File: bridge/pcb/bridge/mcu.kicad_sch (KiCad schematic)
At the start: 12 parts, among them Q1 PMOS, Q2 PMOS, Q3 PMOS, Q4 PMOS, Q5 PMOS, U1 YAAJ_BluePill

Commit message: Fixed issues, added DAC
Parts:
- added R10: 1k5, Resistor_THT:R_Axial_DIN0309_L9.0mm_D3.2mm_P12.70mm_Horizontal, symbol Device:R
- added U3: AD557JN, bridge:AD557JN, symbol bridge:AD557JN
- Q1, Q2, Q3, Q4, Q5: footprint Package_TO_SOT_THT:TO-3P-3_Horizontal_TabDown -> Package_TO_SOT_THT:TO-220-3_Horizontal_TabDown
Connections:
- net +5V: now also U3.11 (+VCC)
- net GND: now also U3.10 (CS*), U3.12 (GND), U3.13 (GND), U3.9 (CE*)
- net at U1.25 (PA0): now also U3.8 ((MSB)BIT1)
- net at U1.26 (PA1): now also U3.7 (BIT2)
- net at U1.27 (PA2): now also U3.6 (BIT3)
- net at U1.28 (PA3): now also U3.5 (BIT4)
- net at U1.29 (PA4): now also U3.4 (BIT5)
- net at U1.30 (PA5): now also U3.3 (BIT6)
- net at U1.31 (PA6): now also U3.2 (BIT7)
- net at U1.32 (PA7): now also U3.1 ((LSB)BIT8)
- new net: R10.2, U3.14 (VOUTSENSEB), U3.15 (VOUTSENSEA)
- new net ACCEL_AUTO: R10.1, U3.16 (VOUT)
- no-connect marks 30 -> 22

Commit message: Completed schematic
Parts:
- R1, R10, R2, R3, R4, R5: footprint Resistor_THT:R_Axial_DIN0309_L9.0mm_D3.2mm_P12.70mm_Horizontal -> bridge:THT_RESISTOR_WITH_VALUE
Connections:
- net MAN_AUTO_STATE: now reaches U1.11 (PB3)
- no-connect marks 22 -> 21
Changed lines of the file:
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@@
   (no_connect (at 130.81 46.99))
   (no_connect (at 90.17 57.15))
-  (no_connect (at 90.17 64.77))
   (no_connect (at 130.81 74.93))
   (no_connect (at 130.81 44.45))
@@
     )
   )
+  (global_label "MAN_AUTO_STATE" (shape input) (at 90.17 64.77 180) (fields_autoplaced)
+    (effects (font (size 1.27 1.27) bold) (justify right))
+    (property "Intersheetrefs" "${INTERSHEET_REFS}" (at 70.8036 64.77 0)
+      (effects (font (size 1.27 1.27)) (justify right) hide)
+    )
+  )
   (global_label "MCU_START" (shape input) (at 57.15 162.56 0) (fields_autoplaced)
     (effects (font (size 1.27 1.27) (thickness 0.254) bold) (justify left))
@@
       (effects (font (size 1.27 1.27)))
     )
-    (property "Footprint" "Resistor_THT:R_Axial_DIN0309_L9.0mm_D3.2mm_P12.70mm_Horizontal" (at 53.34 164.338 90)
+    (property "Footprint" "bridge:THT_RESISTOR_WITH_VALUE" (at 53.34 164.338 90)
       (effects (font (size 1.27 1.27)) hide)
     )
@@
       (effects (font (size 1.27 1.27)))
     )
-    (property "Footprint" "Resistor_THT:R_Axial_DIN0309_L9.0mm_D3.2mm_P12.70mm_Horizontal" (at 53.34 130.048 90)
+    (property "Footprint" "bridge:THT_RESISTOR_WITH_VALUE" (at 53.34 130.048 90)
       (effects (font (size 1.27 1.27)) hide)
     )
@@
       (effects (font (size 1.27 1.27)))
     )
-    (property "Footprint" "Resistor_THT:R_Axial_DIN0309_L9.0mm_D3.2mm_P12.70mm_Horizontal" (at 114.3 164.338 90)
+    (property "Footprint" "bridge:THT_RESISTOR_WITH_VALUE" (at 114.3 164.338 90)
       (effects (font (size 1.27 1.27)) hide)
     )
@@
       (effects (font (size 1.27 1.27)) (justify left))
     )
-    (property "Footprint" "Resistor_THT:R_Axial_DIN0309_L9.0mm_D3.2mm_P12.70mm_Horizontal" (at 226.822 50.8 90)
+    (property "Footprint" "bridge:THT_RESISTOR_WITH_VALUE" (at 226.822 50.8 90)
       (effects (font (size 1.27 1.27)) hide)
     )
@@
       (effects (font (size 1.27 1.27)))
     )
-    (property "Footprint" "Resistor_THT:R_Axial_DIN0309_L9.0mm_D3.2mm_P12.70mm_Horizontal" (at 142.24 126.238 90)
+    (property "Footprint" "bridge:THT_RESISTOR_WITH_VALUE" (at 142.24 126.238 90)
       (effects (font (size 1.27 1.27)) hide)
     )
@@
       (effects (font (size 1.27 1.27)))
     )
-    (property "Footprint" "Resistor_THT:R_Axial_DIN0309_L9.0mm_D3.2mm_P12.70mm_Horizontal" (at 161.29 164.338 90)
-      (effects (font (size 1.27 1.27)) hide)
-    )
+    (property "Footprint" "bridge:THT_RESISTOR_WITH_VALUE" (at 161.29 164.338 90)
+      (effects (font (size 1.27 1.27)) hide)
+    )

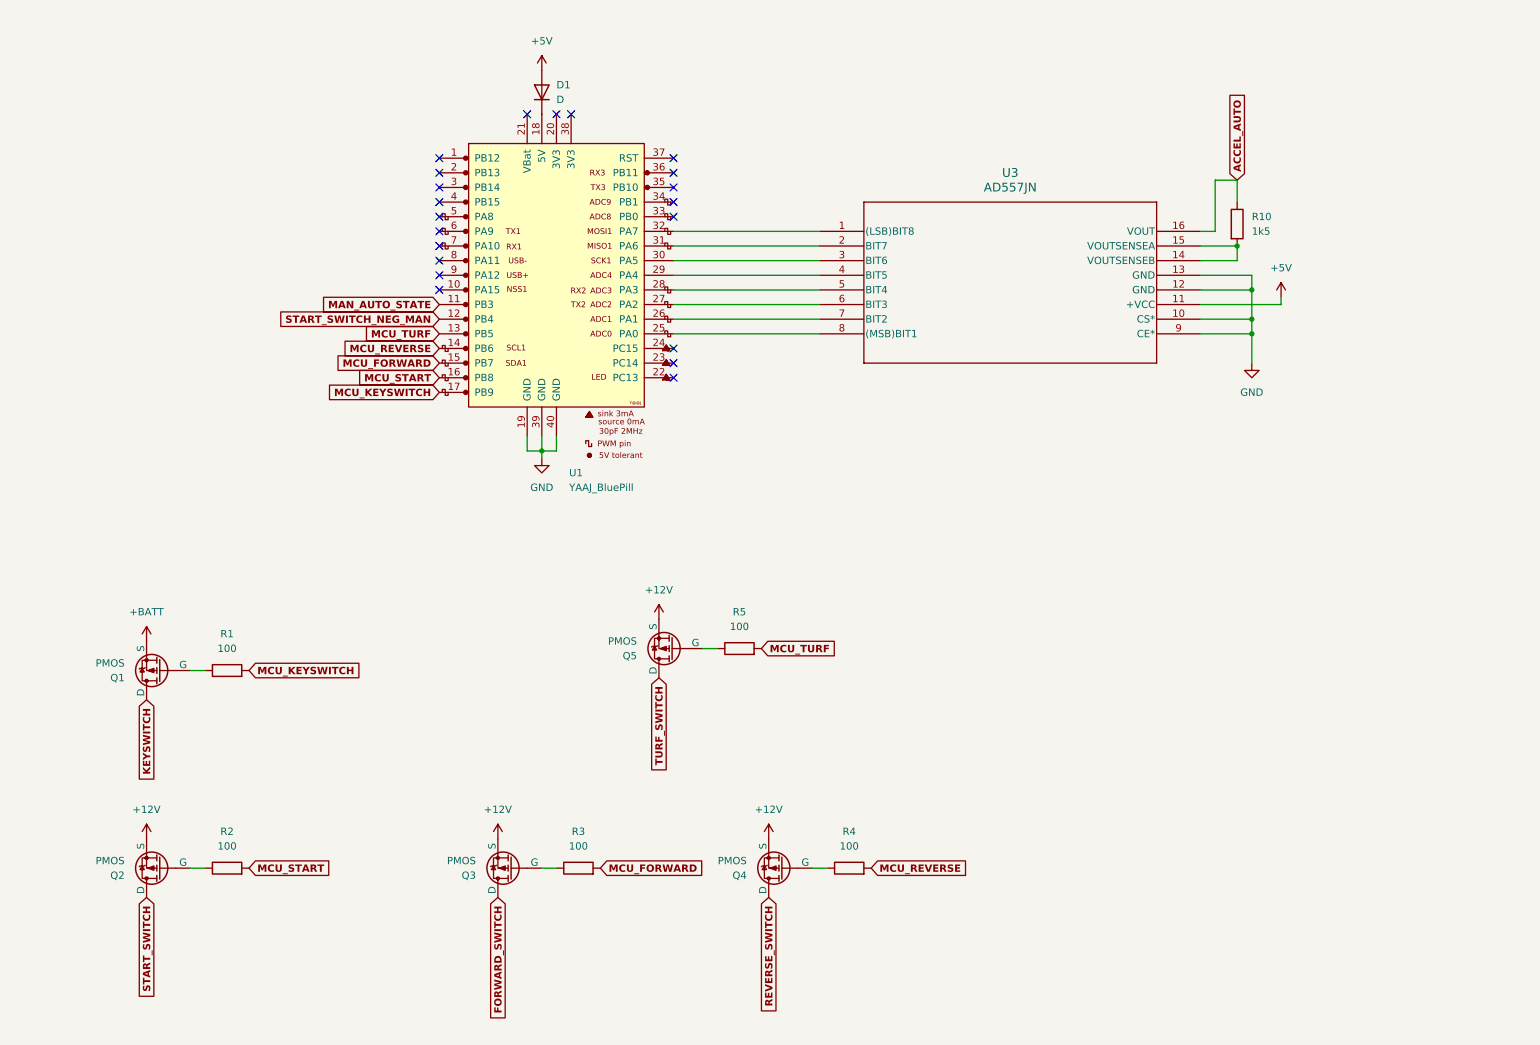
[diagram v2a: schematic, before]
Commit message: Started fixing PCB, reduced footprint and changed MCU
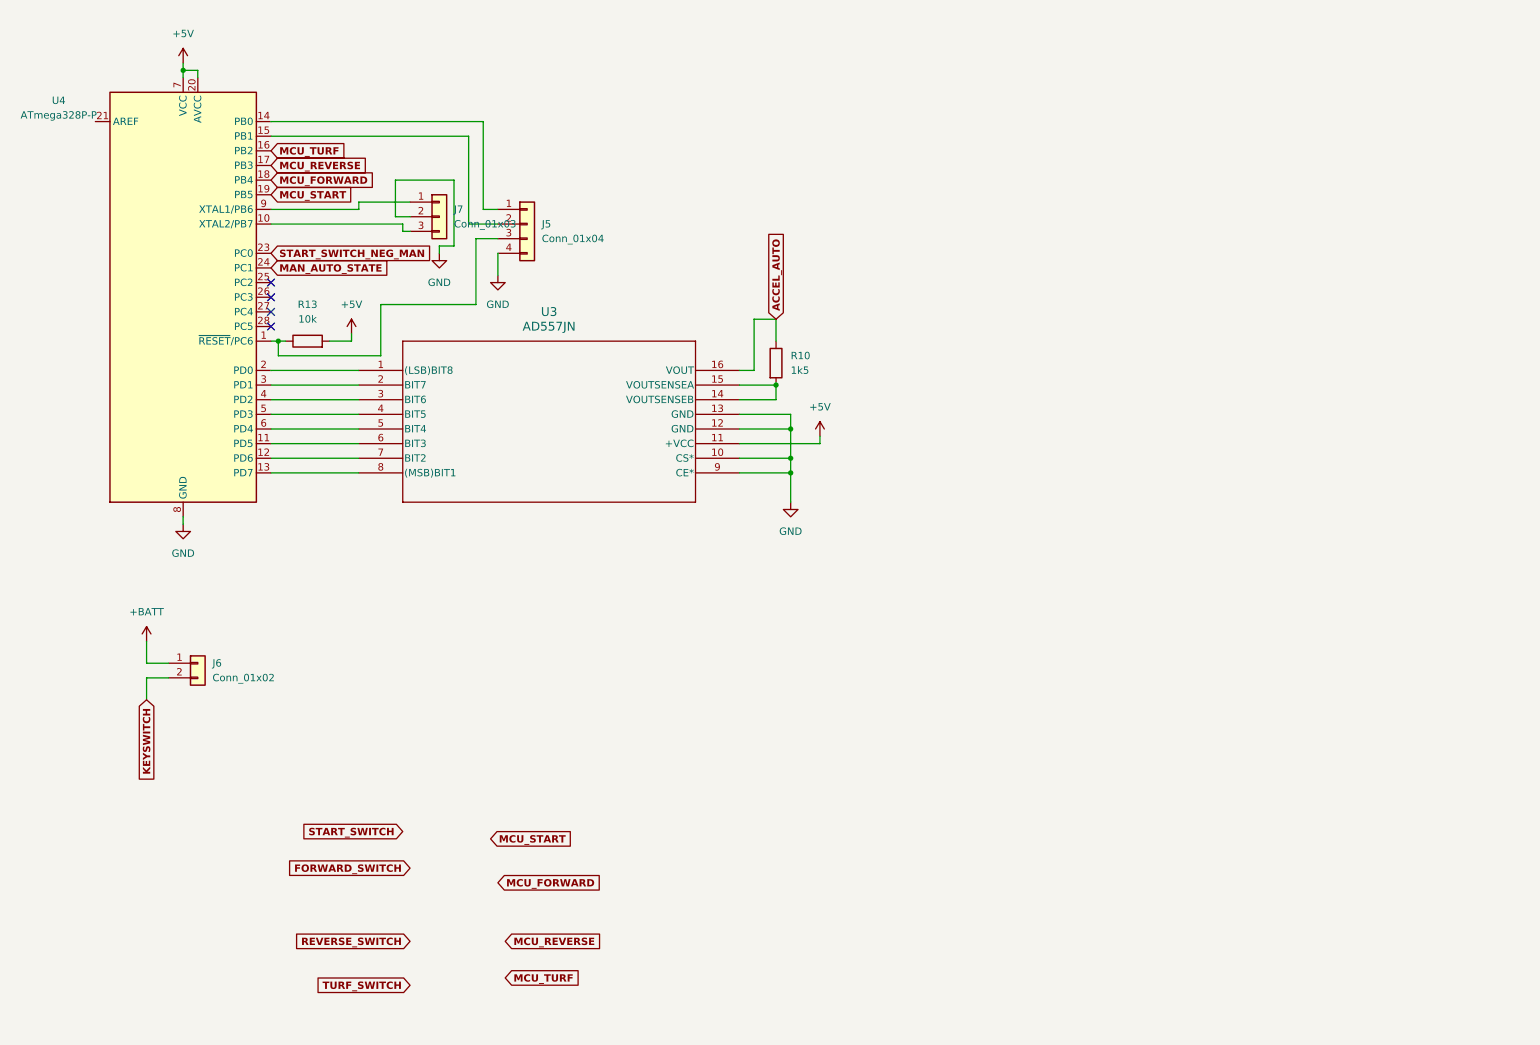
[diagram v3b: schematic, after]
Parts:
- removed D1: D, Diode_THT:D_DO-15_P10.16mm_Horizontal, symbol Device:D
- removed Q1, Q2, Q3, Q4, Q5: PMOS, Package_TO_SOT_THT:TO-220-3_Horizontal_TabDown, symbol Simulation_SPICE:PMOS
- removed R1, R2, R3, R4, R5: 100, bridge:THT_RESISTOR_WITH_VALUE, symbol Device:R
- removed U1: YAAJ_BluePill, bridge:YAAJ_BluePill_1, symbol bridge:YAAJ_BluePill
- added J5: Conn_01x04, Connector_PinHeader_2.54mm:PinHeader_1x04_P2.54mm_Vertical, symbol Connector_Generic:Conn_01x04
- added J6: Conn_01x02, Connector_PinHeader_2.54mm:PinHeader_1x02_P2.54mm_Vertical, symbol Connector_Generic:Conn_01x02
- added J7: Conn_01x03, Connector_PinHeader_2.54mm:PinHeader_1x03_P2.54mm_Vertical, symbol Connector_Generic:Conn_01x03
- added R13: 10k, bridge:THT_RESISTOR_WITH_VALUE, symbol Device:R
- added U4: ATmega328P-P, Package_DIP:DIP-28_W7.62mm, symbol MCU_Microchip_ATmega:ATmega328P-P
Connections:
- net +5V: now also R13.2, U4.20 (AVCC), U4.7 (VCC)
- net +BATT: now also J6.1 (Pin_1)
- net GND: now also J5.4 (Pin_4), J7.2 (Pin_2), U4.22 (GND), U4.8 (GND)
- net KEYSWITCH: now also J6.2 (Pin_2)
- net MAN_AUTO_STATE: now also U4.24 (PC1)
- net MCU_FORWARD: now also U4.18 (PB4)
- net MCU_REVERSE: now also U4.17 (PB3)
- net MCU_START: now also U4.19 (PB5)
- net MCU_TURF: now also U4.16 (PB2)
- net START_SWITCH_NEG_MAN: now also U4.23 (PC0)
- net at U3.8 ((MSB)BIT1): now also U4.13 (PD7)
- net at U3.7 (BIT2): now also U4.12 (PD6)
- net at U3.6 (BIT3): now also U4.11 (PD5)
- net at U3.5 (BIT4): now also U4.6 (PD4)
- net at U3.4 (BIT5): now also U4.5 (PD3)
- net at U3.3 (BIT6): now also U4.4 (PD2)
- net at U3.2 (BIT7): now also U4.3 (PD1)
- net at U3.1 ((LSB)BIT8): now also U4.2 (PD0)
- new net: J7.1 (Pin_1), U4.9 (XTAL1/PB6)
- new net: J7.3 (Pin_3), U4.10 (XTAL2/PB7)
- new net: J5.3 (Pin_3), R13.1, U4.1 (~{RESET}/PC6)
- new net: J5.1 (Pin_1), U4.14 (PB0)
- new net: J5.2 (Pin_2), U4.15 (PB1)
- no-connect marks 21 -> 4
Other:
- moved on the sheet: R10, U3

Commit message: Completed basic functionality PCB
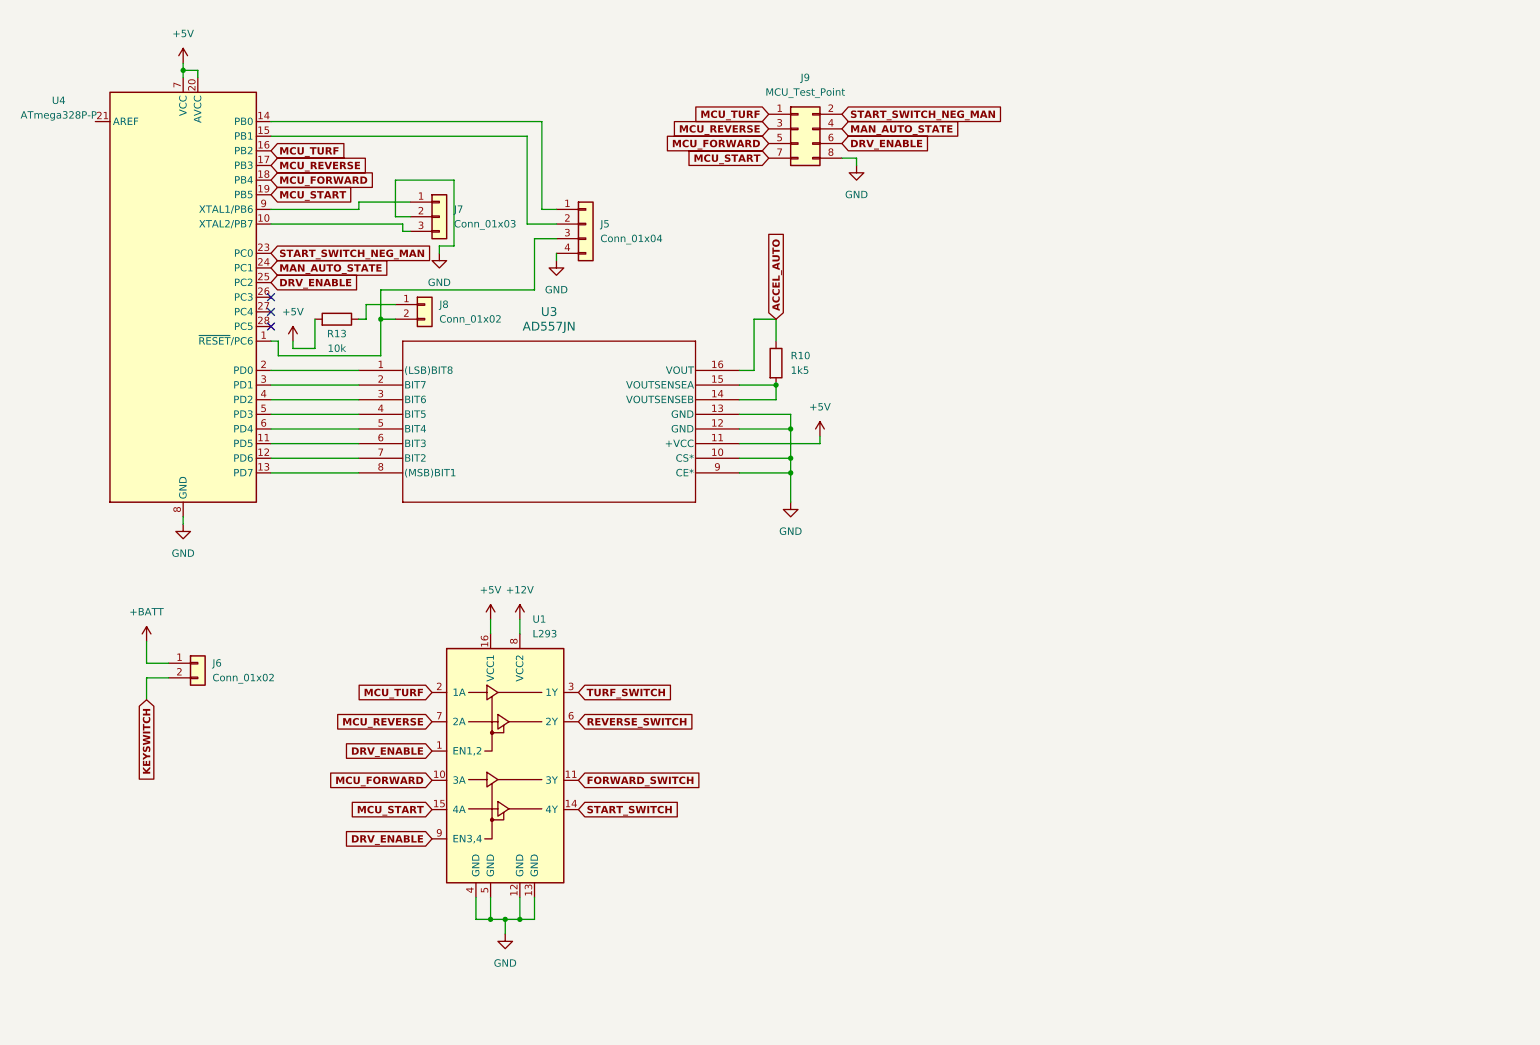
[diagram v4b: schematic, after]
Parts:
- added J8: Conn_01x02, Connector_PinHeader_2.54mm:PinHeader_1x02_P2.54mm_Vertical, symbol Connector_Generic:Conn_01x02
- added J9: MCU_Test_Point, Connector_PinHeader_2.54mm:PinHeader_2x04_P2.54mm_Vertical, symbol Connector_Generic:Conn_02x04_Odd_Even
- added U1: L293, Package_DIP:DIP-16_W7.62mm, symbol Driver_Motor:L293
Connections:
- net +5V: now also U1.16 (VCC1)
- net FORWARD_SWITCH: now also U1.11 (3Y)
- net GND: now also J9.8 (Pin_8), U1.12 (GND), U1.13 (GND), U1.4 (GND), U1.5 (GND)
- net MAN_AUTO_STATE: now also J9.4 (Pin_4)
- net MCU_FORWARD: now also J9.5 (Pin_5), U1.10 (3A)
- net MCU_REVERSE: now also J9.3 (Pin_3), U1.7 (2A)
- net MCU_START: now also J9.7 (Pin_7), U1.15 (4A)
- net MCU_TURF: now also J9.1 (Pin_1), U1.2 (1A)
- net REVERSE_SWITCH: now also U1.6 (2Y)
- net START_SWITCH: now also U1.14 (4Y)
- net START_SWITCH_NEG_MAN: now also J9.2 (Pin_2)
- net TURF_SWITCH: now also U1.3 (1Y)
- net at J5.3 (Pin_3), U4.1 (~{RESET}/PC6): now also J8.2 (Pin_2); no longer R13.1
- net DRV_ENABLE: now reaches U4.25 (PC2)
- net DRV_ENABLE: now also J9.6 (Pin_6), U1.1 (EN1,2), U1.9 (EN3,4)
- new net: J8.1 (Pin_1), R13.1
- new net +12V: U1.8 (VCC2)
- no-connect marks 4 -> 3
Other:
- moved on the sheet: J5, R13

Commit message: Fixed PORTB and PORTD of atmega328p being reversed
Changed RST pin on uart header to be 5V instead and adjusted labels accordingly
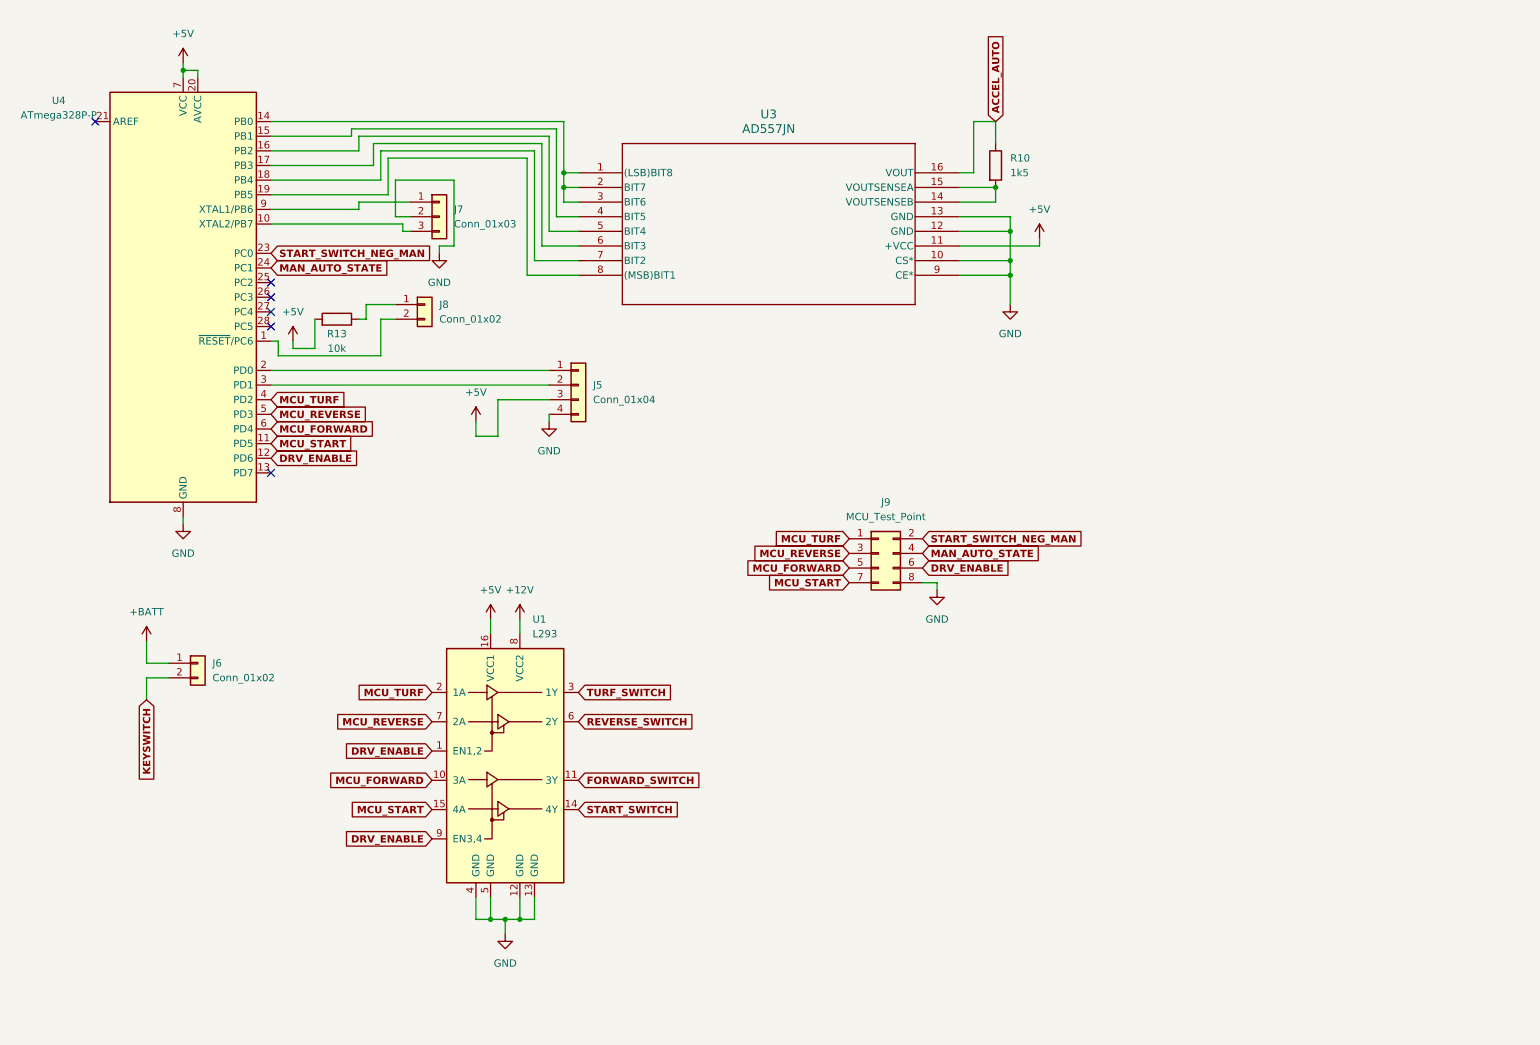
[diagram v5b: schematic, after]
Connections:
- net +5V: now also J5.3 (Pin_3)
- net DRV_ENABLE: now also U4.12 (PD6); no longer U4.25 (PC2)
- net MCU_FORWARD: now also U4.6 (PD4); no longer U4.18 (PB4)
- net MCU_REVERSE: now also U4.5 (PD3); no longer U4.17 (PB3)
- net MCU_START: now also U4.11 (PD5); no longer U4.19 (PB5)
- net MCU_TURF: now also U4.4 (PD2); no longer U4.16 (PB2)
- net at J8.2 (Pin_2), U4.1 (~{RESET}/PC6): no longer J5.3 (Pin_3)
- net at U3.6 (BIT3): now also U4.17 (PB3); no longer U4.11 (PD5)
- net at U3.7 (BIT2): now also U4.18 (PB4); no longer U4.12 (PD6)
- net at U4.13 (PD7): no longer U3.8 ((MSB)BIT1)
- net at U4.14 (PB0): now also U3.1 ((LSB)BIT8), U3.2 (BIT7), U3.3 (BIT6); no longer J5.1 (Pin_1)
- net at U4.15 (PB1): now also U3.4 (BIT5); no longer J5.2 (Pin_2)
- net at U4.2 (PD0): now also J5.1 (Pin_1); no longer U3.1 ((LSB)BIT8)
- net at U4.3 (PD1): now also J5.2 (Pin_2); no longer U3.2 (BIT7)
- net at U3.5 (BIT4): now also U4.16 (PB2); no longer U4.6 (PD4)
- new net: U3.8 ((MSB)BIT1), U4.19 (PB5)
- no-connect marks 3 -> 6
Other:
- moved on the sheet: J5, J9, R10, U3
